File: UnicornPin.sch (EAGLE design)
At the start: 6 parts

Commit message: modified unicorn board
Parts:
- added LED6: (no value), led:LED5MM
- added R1: 120R, resistor:R-US_0207/7
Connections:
- new net N$6: LED1.A, LED6.C
- new net N$7: R1.1, U$1.-
- net N$1: now also LED6.A, R1.2; no longer LED1.A, U$1.-
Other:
- moved on the sheet: LED1
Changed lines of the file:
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@@
 <layer number="97" name="Info" color="7" fill="1" visible="yes" active="yes"/>
 <layer number="98" name="Guide" color="6" fill="1" visible="yes" active="yes"/>
+<layer number="99" name="SpiceOrder" color="5" fill="1" visible="yes" active="yes"/>
 </layers>
 <schematic xreflabel="%F%N/%S.%C%R" xrefpart="/%S.%C%R">
@@
 <part name="LED5" library="led" deviceset="LED" device="3MM"/>
 <part name="U$1" library="battery" deviceset="CR2032-GK" device=""/>
+<part name="LED6" library="led" deviceset="LED" device="5MM"/>
+<part name="R1" library="resistor" deviceset="R-US_" device="0207/7" value="120R"/>
 </parts>
 <sheets>
@@
 </plain>
 <instances>
-<instance part="LED1" gate="G$1" x="38.1" y="68.58" rot="R90"/>
+<instance part="LED1" gate="G$1" x="45.72" y="68.58" rot="R90"/>
 <instance part="LED2" gate="G$1" x="22.86" y="83.82" rot="R90"/>
 <instance part="LED3" gate="G$1" x="33.02" y="83.82" rot="R90"/>
@@
 <instance part="LED5" gate="G$1" x="58.42" y="83.82" rot="R90"/>
 <instance part="U$1" gate="G$1" x="38.1" y="50.8"/>
+<instance part="LED6" gate="G$1" x="30.48" y="68.58" rot="R90"/>
+<instance part="R1" gate="G$1" x="17.78" y="58.42" rot="R90"/>
 </instances>
 <busses>
@@
 <net name="N$1" class="0">
 <segment>
-<pinref part="U$1" gate="G$1" pin="-"/>
-<wire x1="33.02" y1="50.8" x2="17.78" y2="50.8" width="0.1524" layer="91"/>
-<wire x1="17.78" y1="50.8" x2="17.78" y2="68.58" width="0.1524" layer="91"/>
-<pinref part="LED1" gate="G$1" pin="A"/>
-<wire x1="17.78" y1="68.58" x2="35.56" y2="68.58" width="0.1524" layer="91"/>
-<junction x="17.78" y="68.58"/>
+<wire x1="17.78" y1="68.58" x2="27.94" y2="68.58" width="0.1524" layer="91"/>
 <pinref part="LED2" gate="G$1" pin="A"/>
 <wire x1="17.78" y1="83.82" x2="20.32" y2="83.82" width="0.1524" layer="91"/>
 <wire x1="17.78" y1="68.58" x2="17.78" y2="83.82" width="0.1524" layer="91"/>
+<pinref part="LED6" gate="G$1" pin="A"/>
+<pinref part="R1" gate="G$1" pin="2"/>
+<wire x1="17.78" y1="63.5" x2="17.78" y2="68.58" width="0.1524" layer="91"/>
+<junction x="17.78" y="68.58"/>
 </segment>
 </net>
@@
 <wire x1="66.04" y1="50.8" x2="66.04" y2="68.58" width="0.1524" layer="91"/>
 <pinref part="LED1" gate="G$1" pin="C"/>
-<wire x1="66.04" y1="68.58" x2="43.18" y2="68.58" width="0.1524" layer="91"/>
+<wire x1="66.04" y1="68.58" x2="50.8" y2="68.58" width="0.1524" layer="91"/>
 <pinref part="LED5" gate="G$1" pin="C"/>
 <wire x1="63.5" y1="83.82" x2="66.04" y2="83.82" width="0.1524" layer="91"/>
@@
 </segment>
 </net>
+<net name="N$6" class="0">
+<segment>
+<pinref part="LED1" gate="G$1" pin="A"/>
+<wire x1="35.56" y1="68.58" x2="43.18" y2="68.58" width="0.1524" layer="91"/>
+<pinref part="LED6" gate="G$1" pin="C"/>
+</segment>
+</net>
+<net name="N$7" class="0">
+<segment>
+<pinref part="U$1" gate="G$1" pin="-"/>
+<wire x1="33.02" y1="50.8" x2="17.78" y2="50.8" width="0.1524" layer="91"/>
+<pinref part="R1" gate="G$1" pin="1"/>
+<wire x1="17.78" y1="50.8" x2="17.78" y2="53.34" width="0.1524" layer="91"/>
+</segment>
+</net>

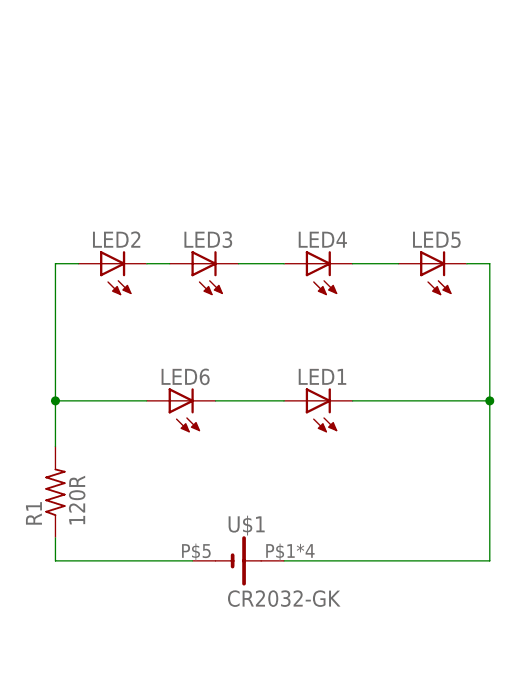
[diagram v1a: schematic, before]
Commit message: changed unicorn schematic so that all leds are in parallel with each other
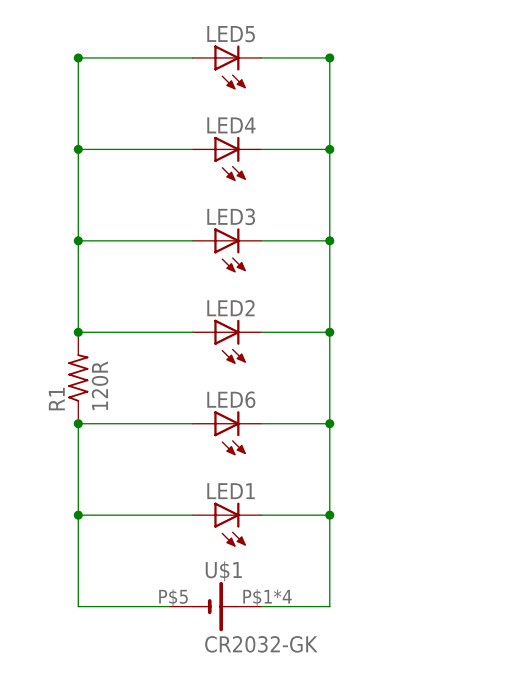
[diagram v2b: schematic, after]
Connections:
- removed net N$4: LED3.C, LED4.A
- removed net N$5: LED4.C, LED5.A
- removed net N$6: LED1.A, LED6.C
- removed net N$7: R1.1, U$1.-
- net N$1: now also LED1.A, R1.1, U$1.-; no longer LED2.A, R1.2
- net N$2: now also LED2.C, LED3.C, LED4.C, LED6.C
- net N$3: now also LED2.A, LED4.A, LED5.A, R1.2; no longer LED2.C
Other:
- moved on the sheet: LED1, LED2, LED3, LED4, LED5, LED6, R1, U$1
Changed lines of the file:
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@@
 </plain>
 <instances>
-<instance part="LED1" gate="G$1" x="45.72" y="68.58" rot="R90"/>
-<instance part="LED2" gate="G$1" x="22.86" y="83.82" rot="R90"/>
-<instance part="LED3" gate="G$1" x="33.02" y="83.82" rot="R90"/>
-<instance part="LED4" gate="G$1" x="45.72" y="83.82" rot="R90"/>
-<instance part="LED5" gate="G$1" x="58.42" y="83.82" rot="R90"/>
-<instance part="U$1" gate="G$1" x="38.1" y="50.8"/>
-<instance part="LED6" gate="G$1" x="30.48" y="68.58" rot="R90"/>
-<instance part="R1" gate="G$1" x="17.78" y="58.42" rot="R90"/>
+<instance part="LED1" gate="G$1" x="35.56" y="55.88" rot="R90"/>
+<instance part="LED2" gate="G$1" x="35.56" y="76.2" rot="R90"/>
+<instance part="LED3" gate="G$1" x="35.56" y="86.36" rot="R90"/>
+<instance part="LED4" gate="G$1" x="35.56" y="96.52" rot="R90"/>
+<instance part="LED5" gate="G$1" x="35.56" y="106.68" rot="R90"/>
+<instance part="U$1" gate="G$1" x="35.56" y="45.72"/>
+<instance part="LED6" gate="G$1" x="35.56" y="66.04" rot="R90"/>
+<instance part="R1" gate="G$1" x="20.32" y="71.12" rot="R90"/>
 </instances>
 <busses>
@@
 <net name="N$1" class="0">
 <segment>
-<wire x1="17.78" y1="68.58" x2="27.94" y2="68.58" width="0.1524" layer="91"/>
-<pinref part="LED2" gate="G$1" pin="A"/>
-<wire x1="17.78" y1="83.82" x2="20.32" y2="83.82" width="0.1524" layer="91"/>
-<wire x1="17.78" y1="68.58" x2="17.78" y2="83.82" width="0.1524" layer="91"/>
+<pinref part="U$1" gate="G$1" pin="-"/>
+<wire x1="30.48" y1="45.72" x2="20.32" y2="45.72" width="0.1524" layer="91"/>
+<wire x1="20.32" y1="45.72" x2="20.32" y2="55.88" width="0.1524" layer="91"/>
+<pinref part="LED1" gate="G$1" pin="A"/>
+<wire x1="20.32" y1="55.88" x2="33.02" y2="55.88" width="0.1524" layer="91"/>
+<junction x="20.32" y="55.88"/>
+<wire x1="20.32" y1="55.88" x2="20.32" y2="66.04" width="0.1524" layer="91"/>
 <pinref part="LED6" gate="G$1" pin="A"/>
-<pinref part="R1" gate="G$1" pin="2"/>
-<wire x1="17.78" y1="63.5" x2="17.78" y2="68.58" width="0.1524" layer="91"/>
-<junction x="17.78" y="68.58"/>
+<wire x1="20.32" y1="66.04" x2="33.02" y2="66.04" width="0.1524" layer="91"/>
+<pinref part="R1" gate="G$1" pin="1"/>
+<junction x="20.32" y="66.04"/>
 </segment>
 </net>
@@
 <segment>
 <pinref part="U$1" gate="G$1" pin="+"/>
-<wire x1="43.18" y1="50.8" x2="66.04" y2="50.8" width="0.1524" layer="91"/>
-<wire x1="66.04" y1="50.8" x2="66.04" y2="68.58" width="0.1524" layer="91"/>
+<wire x1="40.64" y1="45.72" x2="48.26" y2="45.72" width="0.1524" layer="91"/>
+<wire x1="48.26" y1="45.72" x2="48.26" y2="55.88" width="0.1524" layer="91"/>
 <pinref part="LED1" gate="G$1" pin="C"/>
-<wire x1="66.04" y1="68.58" x2="50.8" y2="68.58" width="0.1524" layer="91"/>
+<wire x1="48.26" y1="55.88" x2="40.64" y2="55.88" width="0.1524" layer="91"/>
+<junction x="48.26" y="55.88"/>
+<pinref part="LED6" gate="G$1" pin="C"/>
+<wire x1="40.64" y1="66.04" x2="48.26" y2="66.04" width="0.1524" layer="91"/>
+<wire x1="48.26" y1="66.04" x2="48.26" y2="55.88" width="0.1524" layer="91"/>
+<junction x="48.26" y="66.04"/>
+<pinref part="LED2" gate="G$1" pin="C"/>
+<wire x1="40.64" y1="76.2" x2="48.26" y2="76.2" width="0.1524" layer="91"/>
+<wire x1="48.26" y1="76.2" x2="48.26" y2="66.04" width="0.1524" layer="91"/>
+<junction x="48.26" y="76.2"/>
+<wire x1="48.26" y1="76.2" x2="48.26" y2="86.36" width="0.1524" layer="91"/>
+<pinref part="LED3" gate="G$1" pin="C"/>
+<wire x1="48.26" y1="86.36" x2="40.64" y2="86.36" width="0.1524" layer="91"/>
+<junction x="48.26" y="86.36"/>
+<wire x1="48.26" y1="86.36" x2="48.26" y2="96.52" width="0.1524" layer="91"/>
+<pinref part="LED4" gate="G$1" pin="C"/>
+<wire x1="48.26" y1="96.52" x2="40.64" y2="96.52" width="0.1524" layer="91"/>
+<junction x="48.26" y="96.52"/>
+<wire x1="48.26" y1="96.52" x2="48.26" y2="106.68" width="0.1524" layer="91"/>
 <pinref part="LED5" gate="G$1" pin="C"/>
-<wire x1="63.5" y1="83.82" x2="66.04" y2="83.82" width="0.1524" layer="91"/>
-<wire x1="66.04" y1="83.82" x2="66.04" y2="68.58" width="0.1524" layer="91"/>
-<junction x="66.04" y="68.58"/>
+<wire x1="48.26" y1="106.68" x2="40.64" y2="106.68" width="0.1524" layer="91"/>
+<junction x="48.26" y="106.68"/>
 </segment>
 </net>
 <net name="N$3" class="0">
 <segment>
-<pinref part="LED2" gate="G$1" pin="C"/>
+<pinref part="LED5" gate="G$1" pin="A"/>
+<wire x1="33.02" y1="106.68" x2="20.32" y2="106.68" width="0.1524" layer="91"/>
+<pinref part="LED2" gate="G$1" pin="A"/>
+<pinref part="R1" gate="G$1" pin="2"/>
+<wire x1="33.02" y1="76.2" x2="20.32" y2="76.2" width="0.1524" layer="91"/>
+<wire x1="20.32" y1="76.2" x2="20.32" y2="86.36" width="0.1524" layer="91"/>
 <pinref part="LED3" gate="G$1" pin="A"/>
-<wire x1="27.94" y1="83.82" x2="30.48" y2="83.82" width="0.1524" layer="91"/>
+<wire x1="20.32" y1="86.36" x2="33.02" y2="86.36" width="0.1524" layer="91"/>
+<junction x="20.32" y="76.2"/>
+<junction x="20.32" y="86.36"/>
+<wire x1="20.32" y1="86.36" x2="20.32" y2="96.52" width="0.1524" layer="91"/>
+<pinref part="LED4" gate="G$1" pin="A"/>
+<wire x1="20.32" y1="96.52" x2="33.02" y2="96.52" width="0.1524" layer="91"/>
+<junction x="20.32" y="96.52"/>
+<wire x1="20.32" y1="96.52" x2="20.32" y2="106.68" width="0.1524" layer="91"/>
+<junction x="20.32" y="106.68"/>
 </segment>
 </net>
-<net name="N$4" class="0">
-<segment>
-<pinref part="LED3" gate="G$1" pin="C"/>
-<pinref part="LED4" gate="G$1" pin="A"/>
-<wire x1="38.1" y1="83.82" x2="43.18" y2="83.82" width="0.1524" layer="91"/>
-</segment>
-</net>
-<net name="N$5" class="0">
-<segment>
-<pinref part="LED4" gate="G$1" pin="C"/>
-<pinref part="LED5" gate="G$1" pin="A"/>
-<wire x1="50.8" y1="83.82" x2="55.88" y2="83.82" width="0.1524" layer="91"/>
-</segment>
-</net>
-<net name="N$6" class="0">
-<segment>
-<pinref part="LED1" gate="G$1" pin="A"/>
-<wire x1="35.56" y1="68.58" x2="43.18" y2="68.58" width="0.1524" layer="91"/>
-<pinref part="LED6" gate="G$1" pin="C"/>
-</segment>
-</net>
-<net name="N$7" class="0">
-<segment>
-<pinref part="U$1" gate="G$1" pin="-"/>
-<wire x1="33.02" y1="50.8" x2="17.78" y2="50.8" width="0.1524" layer="91"/>
-<pinref part="R1" gate="G$1" pin="1"/>
-<wire x1="17.78" y1="50.8" x2="17.78" y2="53.34" width="0.1524" layer="91"/>
-</segment>
-</net>
